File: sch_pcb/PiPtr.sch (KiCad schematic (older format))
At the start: 69 parts, among them J101 GLOBAL LINK 1 LEFT, J102 GLOBAL LINK 1 RIGHT, J104 GLOBAL LINK 2 LEFT, J106 GLOBAL LINK 2 RIGHT, J107 RASPBERRY_PI, J111 FP_PIXEL, J112 AM2302, J113 I2C1_5V, J114 I2C0_3v3, J117 OLED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

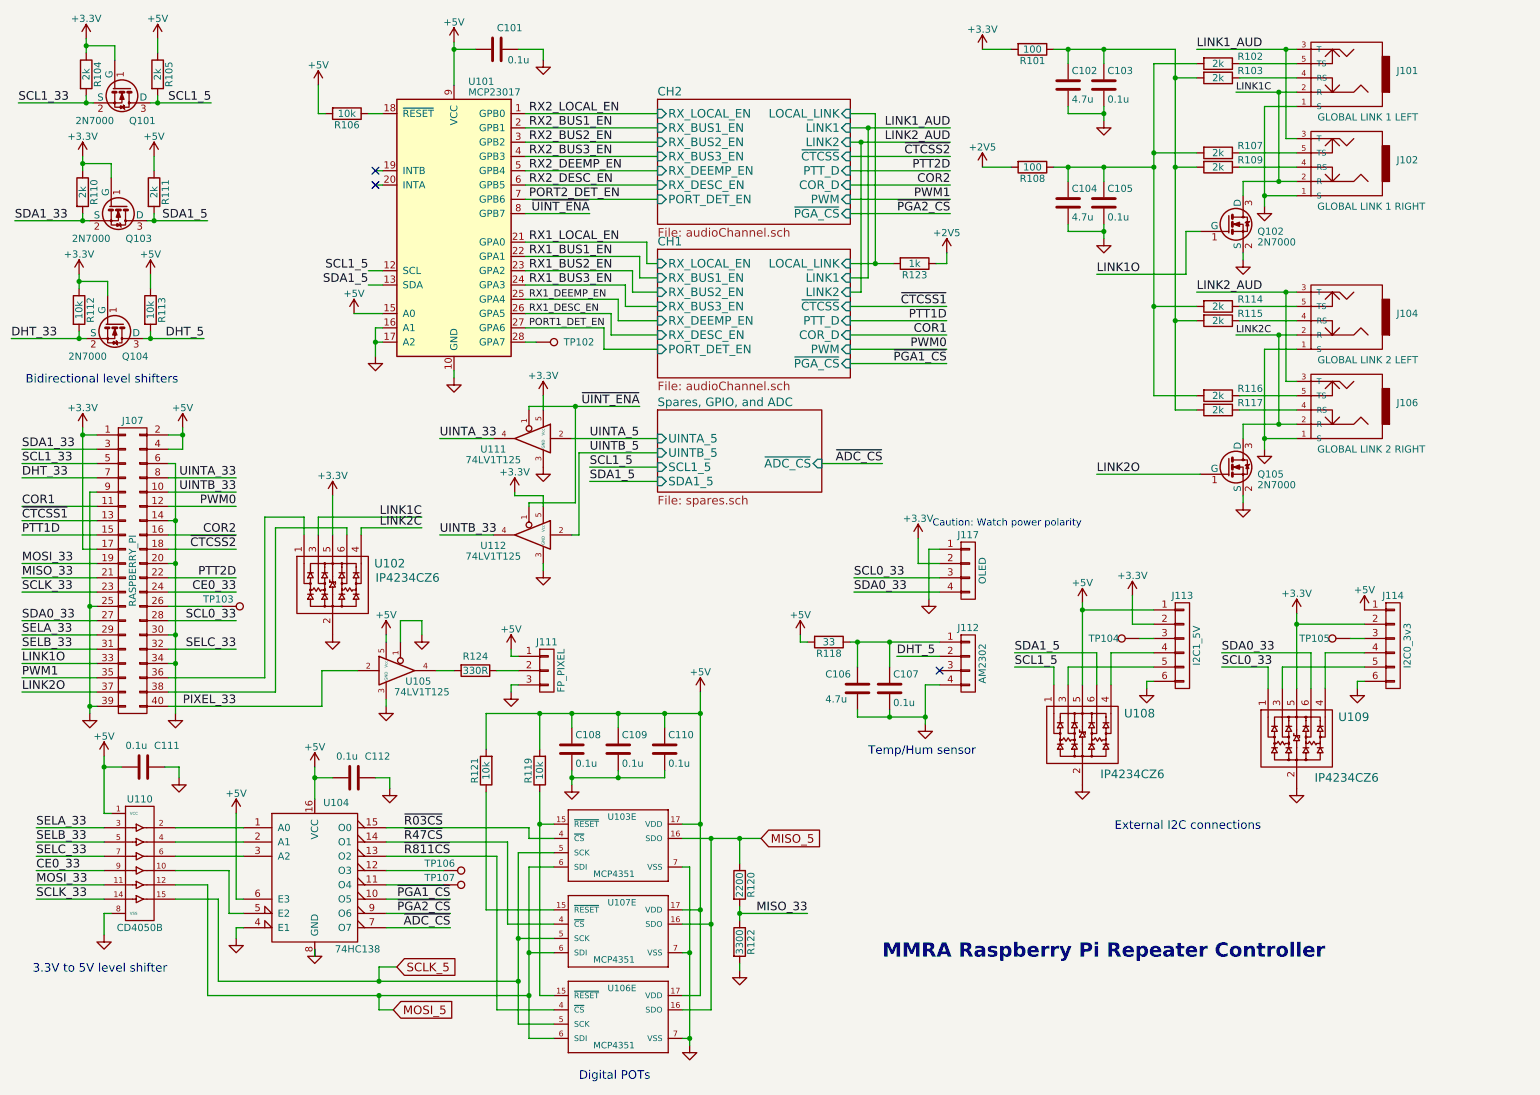
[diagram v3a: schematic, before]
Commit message: Add files via upload
Change link connectors to use a daughterboard for the off-rack links and 100mil headers for between-board links
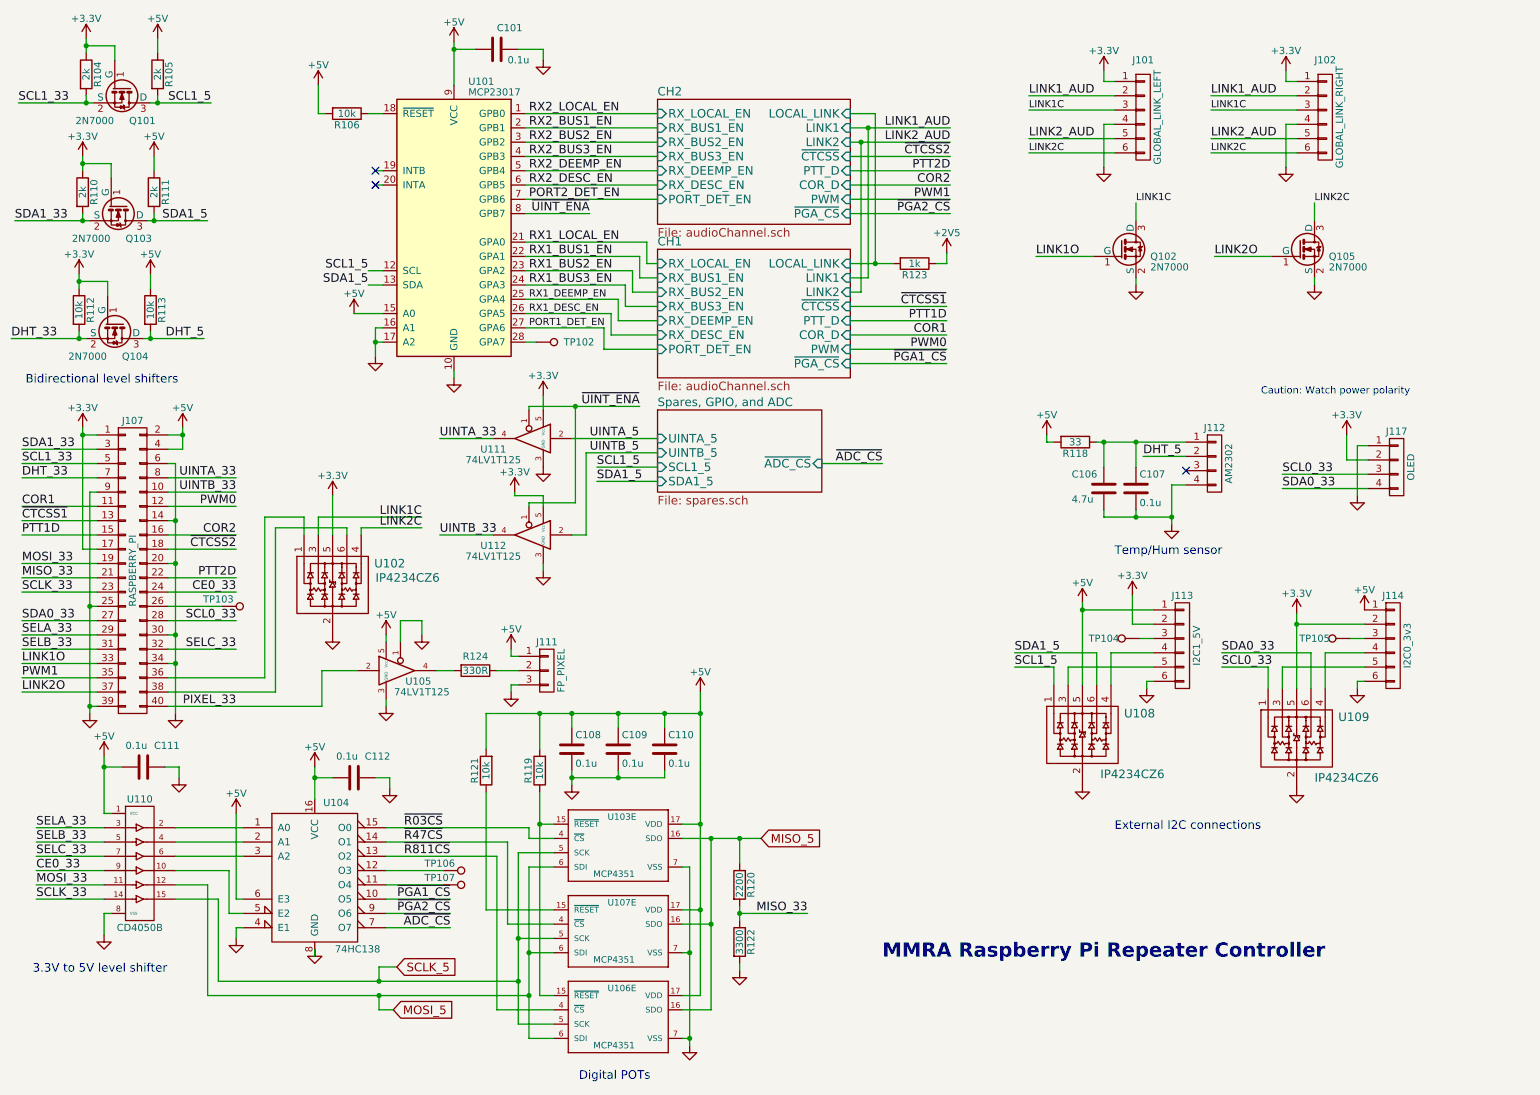
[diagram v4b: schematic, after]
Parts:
- removed C102, C104: 4.7u, lib:smd0603, symbol C
- removed C103, C105: 0.1u, lib:smd0603, symbol C
- removed J101: GLOBAL LINK 1 LEFT, lib:TRS3.5_5, symbol JACK_TRS
- removed J102: GLOBAL LINK 1 RIGHT, lib:TRS3.5_5, symbol JACK_TRS
- removed J104: GLOBAL LINK 2 LEFT, lib:TRS3.5_5, symbol JACK_TRS
- removed J106: GLOBAL LINK 2 RIGHT, lib:TRS3.5_5, symbol JACK_TRS
- removed R101, R108: 100, lib:smd0603, symbol R
- removed R102, R103, R107, R109, R114, R115, R116, R117: 2k, lib:smd0603, symbol R
- added J101: GLOBAL_LINK_LEFT, lib:Molex_22-27-2061_100mil_6pin_verical, symbol CONN_01X06
- added J102: GLOBAL_LINK_RIGHT, lib:Molex_22-27-2061_100mil_6pin_verical, symbol CONN_01X06
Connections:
- net +3V3: now also J101.1 (P1), J102.1 (P1)
- net GND: now also J101.4 (P4), J102.4 (P4)
- net LINK1C: now also J101.3 (P3), J102.3 (P3)
- net LINK1_AUD: now also J101.2 (P2), J102.2 (P2)
- net LINK2C: now also J101.6 (P6), J102.6 (P6)
- net LINK2_AUD: now also J101.5 (P5), J102.5 (P5)
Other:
- moved on the sheet: C106, C107, J112, J117, Q102, Q105, R118

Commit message: Add soundcard schematic
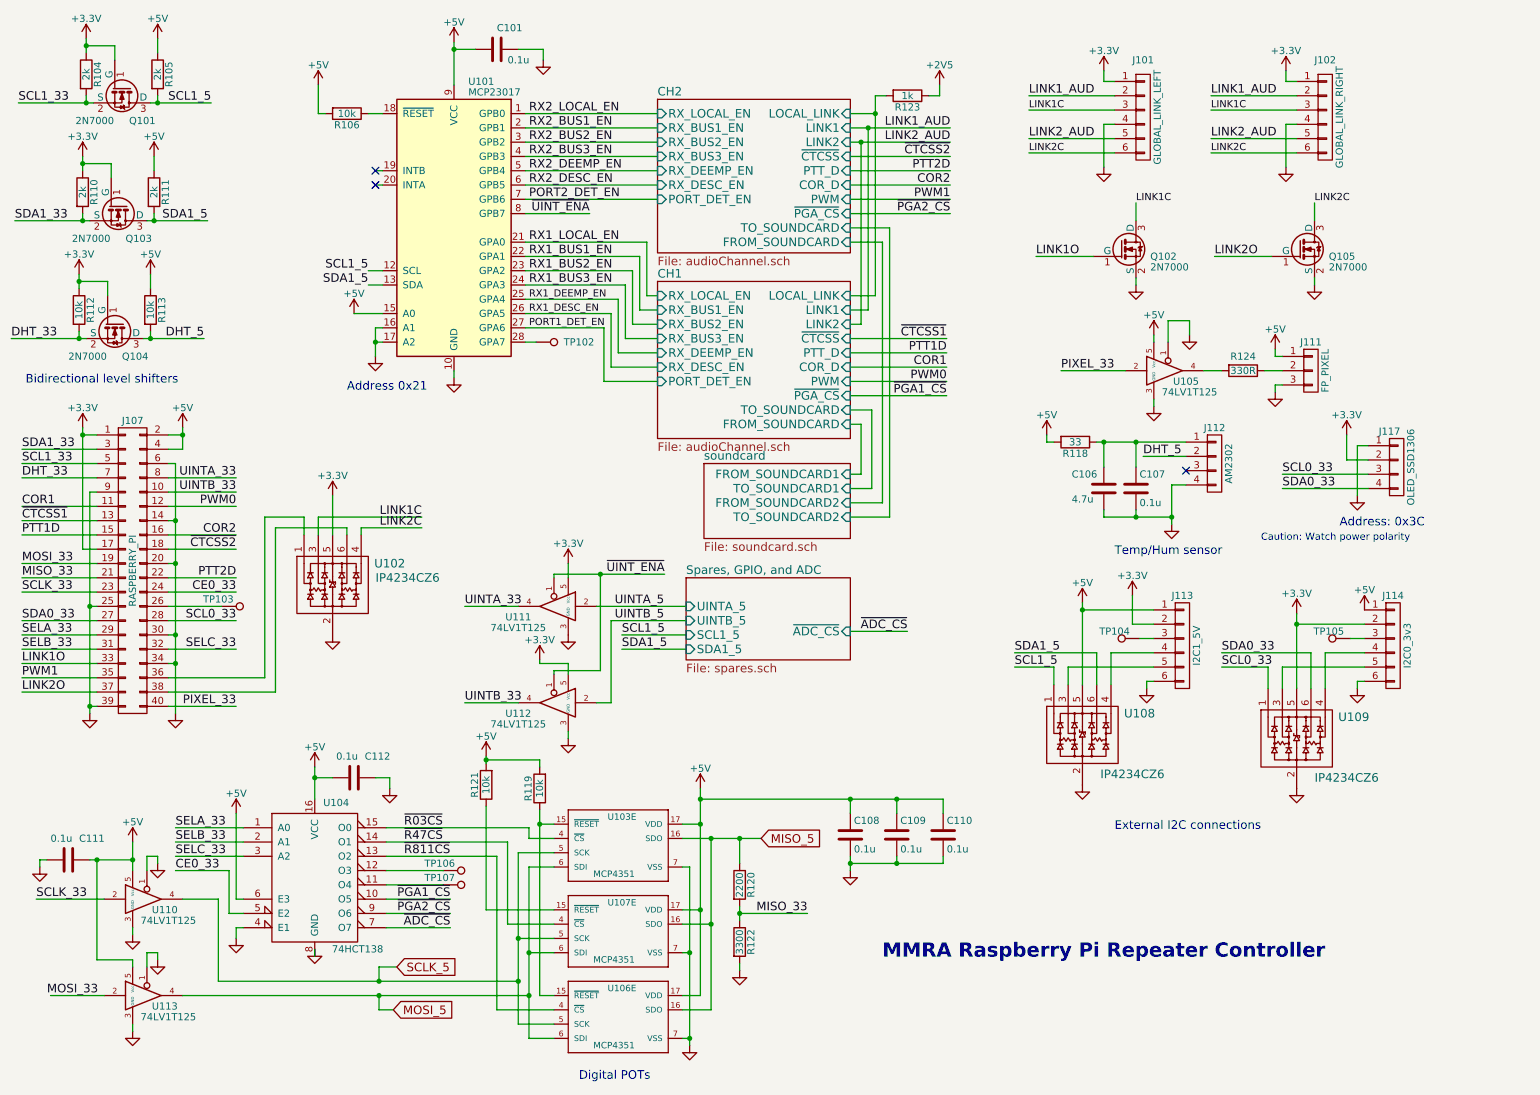
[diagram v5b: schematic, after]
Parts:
- removed U110: CD4050B, lib:SOIC16, symbol CD4050B_1piece
- added U110, U113: 74LV1T125, lib:SOT23-5, symbol 74LVC1G125
- J117: value OLED -> OLED_SSD1306
- U104: value 74HC138 -> 74HCT138
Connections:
- net +5V: now also C111.1, U110.5 (Vcc), U113.5 (Vcc); no longer C111.2
- net CE0_33: now also U104.5 (E2)
- net GND: now also C111.2, U110.1, U110.3 (GND), U113.1, U113.3 (GND); no longer C111.1
- net MOSI_5: now also U113.4
- net SCLK_33: now also U110.2
- net SCLK_5: now also U110.4
- net SELA_33: now also U104.1 (A0)
- net SELB_33: now also U104.2 (A1)
- net SELC_33: now also U104.3 (A2)
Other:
- note added: "Address 0x21"
- note added: "Address: 0x3C"
- note removed: "3.3V to 5V level shifter"
- moved on the sheet: C108, C109, C110, C111, J111, R119, R121, R123, R124, U105, U111, U112

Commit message: Update from latest round of emails
Change connectors - use correct footprint for DE9F.  Add chassis connector as DE9M, AUX_IO connectors as 116-pin ribbon, expected to transition to DA15 with a cable.  
Remove screw terminals for 12V input as it now comes in on chassis connector
Remove third EEPOT package
Move stuff off PCB in preparation to incorporate all the schematic updates.
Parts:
- removed U106: MCP4351, lib:SSOP-20, symbol MCP344XD
- Q101, Q102, Q103, Q104, Q105: value 2N7000 -> BSS138
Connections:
- net MOSI_33: now also U113.2
- net SCL0_33: no longer J117.3 (P3)
- net SCL1_33: now also J117.3 (P3)
- net SDA0_33: no longer J117.4 (P4)
- net SDA1_33: now also J117.4 (P4)
- net ~R811CS: no longer names the net of U104.13 (O2)
- no-connect marks 3 -> 4

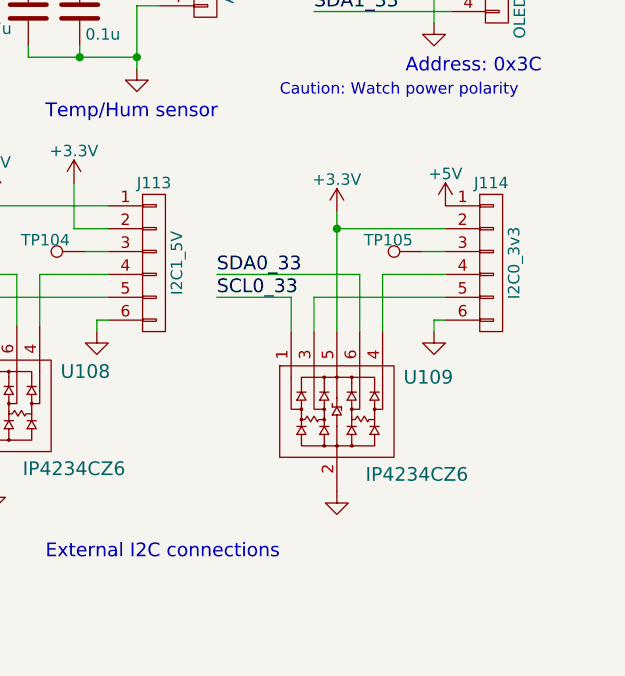
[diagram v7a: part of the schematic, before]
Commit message: Add files via upload
More routing of the PCB....  Slowly getting there.
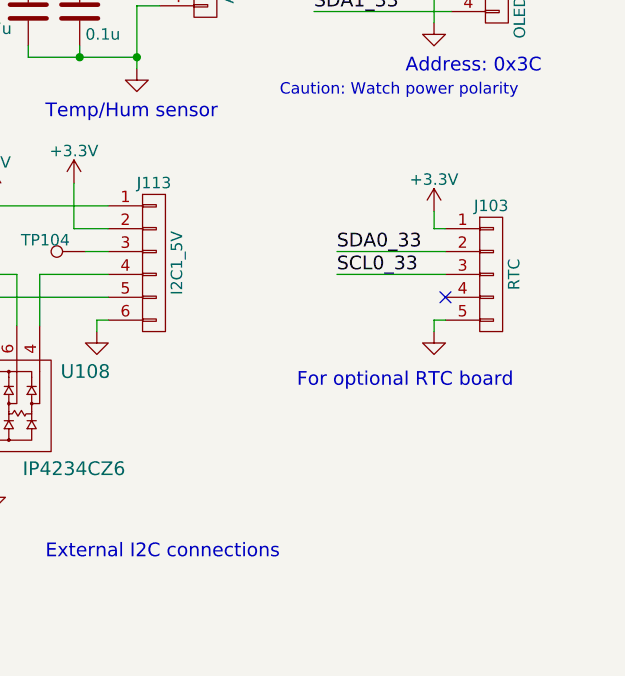
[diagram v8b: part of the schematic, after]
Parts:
- removed J114: I2C0_3v3, lib:SIL-6, symbol CONN_01X06
- removed TP105: TESTPOINT, lib:Wire_28AWG, symbol TESTPOINT
- removed U109: IP4234CZ6, lib:SOT23-6, symbol IP4234CZ6_USB_ESD_PROTECTOR
- added J103: RTC, symbol CONN_01X05
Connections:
- net +3V3: now also J103.1 (P1)
- net GND: now also J103.5 (P5)
- net SCL0_33: now also J103.3 (P3)
- net SDA0_33: now also J103.2 (P2)
- no-connect marks 4 -> 5
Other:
- note added: "For optional RTC board"
